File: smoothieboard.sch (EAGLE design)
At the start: 235 parts, among them IC1 LPC1769, IC10 LM1117-3.3V, IC11 78L12F, IC2 A4982, IC3 A4982, IC4 MCP44X1, IC5 A4982, IC6 A4982, J10 POWER_JACKSMD, Q1 BSL207SP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

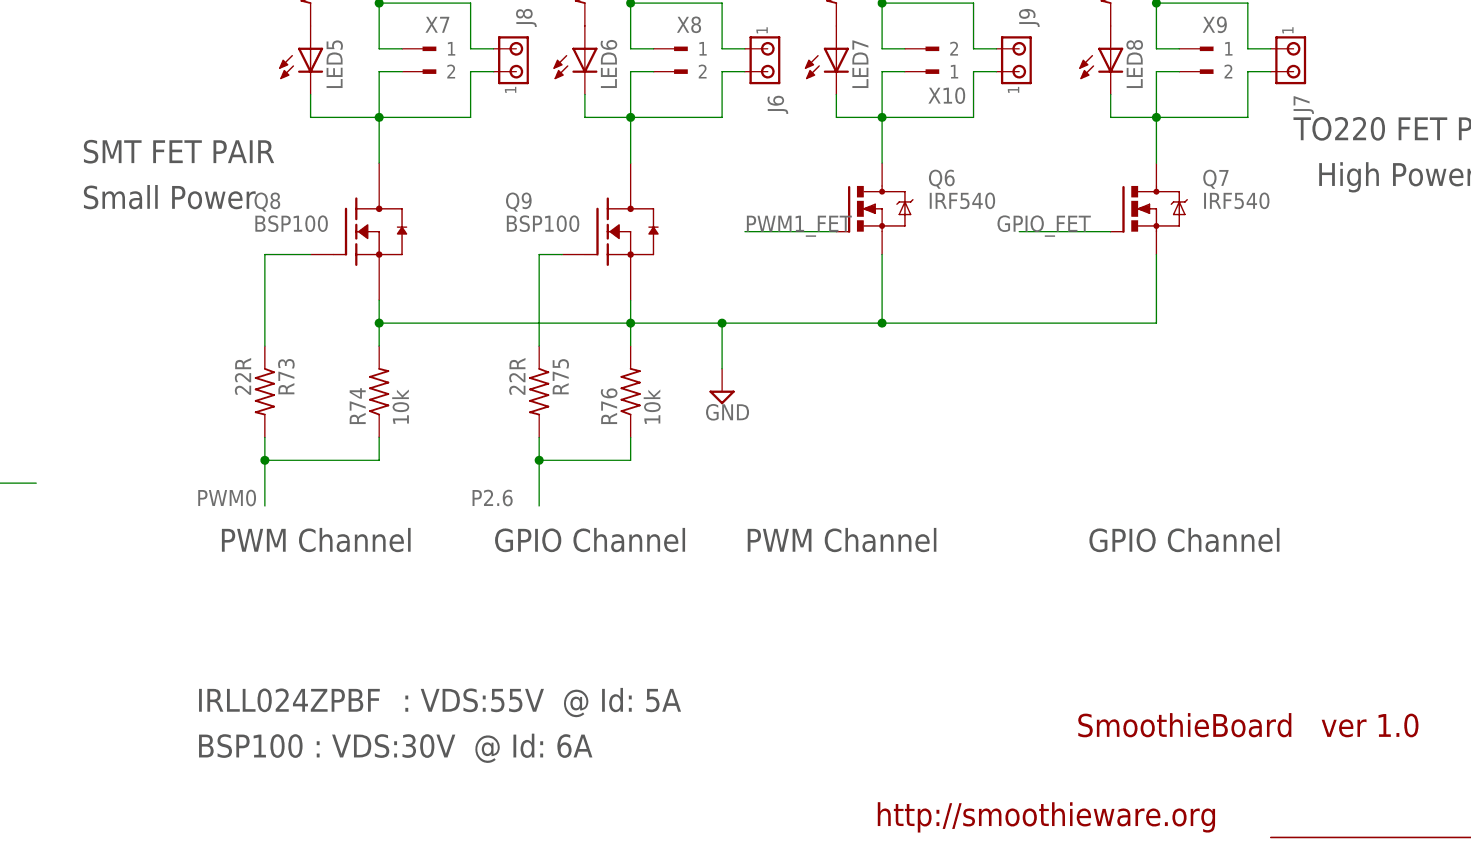
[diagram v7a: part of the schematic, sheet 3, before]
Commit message: Fixed MOSFET labels on schematic to match BOM
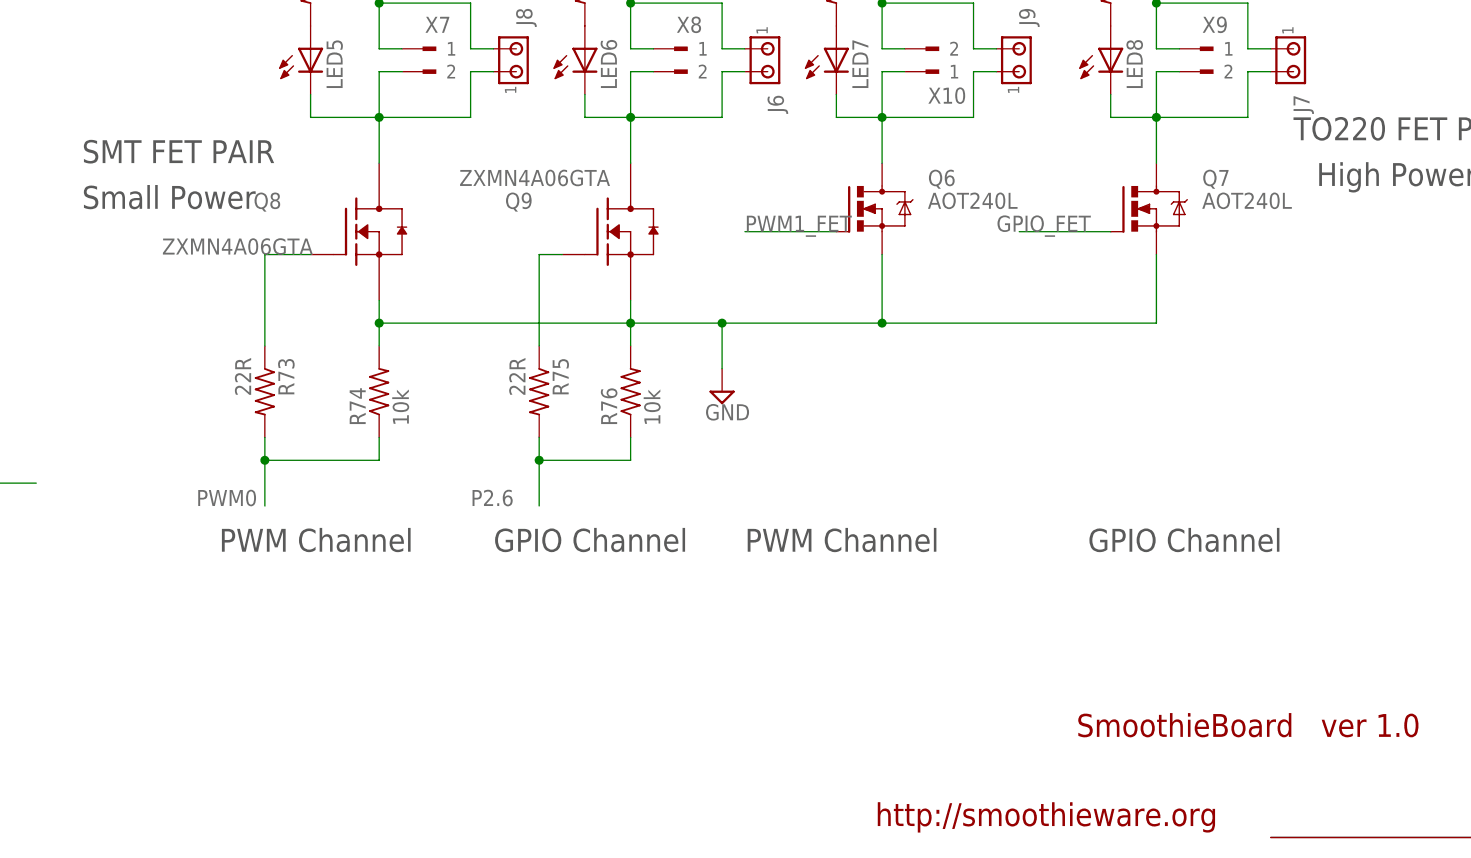
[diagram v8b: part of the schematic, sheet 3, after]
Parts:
- Q6, Q7: value IRF540 -> AOT240L
- Q8, Q9: value BSP100 -> ZXMN4A06GTA
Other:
- note removed: ": VDS:55V @ Id: 5A"
- note removed: "BSP100 : VDS:30V @ Id: 6A"
- note removed: "IRLL024ZPBF"
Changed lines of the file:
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@@
 <part name="LED9" library="led" deviceset="LED" device="CHIP-LED0805"/>
 <part name="R77" library="resistor" deviceset="R-US_" device="R0603" value="1k"/>
-<part name="Q6" library="transistor-power" deviceset="IRF540" device=""/>
-<part name="Q7" library="transistor-power" deviceset="IRF540" device=""/>
+<part name="Q6" library="transistor-power" deviceset="IRF540" device="" value="AOT240L"/>
+<part name="Q7" library="transistor-power" deviceset="IRF540" device="" value="AOT240L"/>
 <part name="SUPPLY18" library="supply2" deviceset="GND" device=""/>
 <part name="R73" library="resistor" deviceset="R-US_" device="R0603" value="22R"/>
@@
 <part name="R78" library="resistor" deviceset="R-US_" device="R0603" value="2.2K"/>
 <part name="LED10" library="led" deviceset="LED" device="CHIP-LED0805"/>
-<part name="Q8" library="ipc-7351-transistor" deviceset="MOSFET-NCH_" device="SOT-223" value="BSP100"/>
-<part name="Q9" library="ipc-7351-transistor" deviceset="MOSFET-NCH_" device="SOT-223" value="BSP100"/>
+<part name="Q8" library="ipc-7351-transistor" deviceset="MOSFET-NCH_" device="SOT-223" value="ZXMN4A06GTA"/>
+<part name="Q9" library="ipc-7351-transistor" deviceset="MOSFET-NCH_" device="SOT-223" value="ZXMN4A06GTA"/>
 <part name="R74" library="resistor" deviceset="R-US_" device="R0603" value="10k"/>
 <part name="R76" library="resistor" deviceset="R-US_" device="R0603" value="10k"/>
@@
 <text x="322.58" y="35.56" size="2.54" layer="97">GPIO Channel</text>
 <text x="284.48" y="35.56" size="2.54" layer="97">PWM Channel</text>
-<text x="223.52" y="17.78" size="2.54" layer="97">IRLL024ZPBF </text>
-<text x="246.38" y="17.78" size="2.54" layer="97">: VDS:55V  @ Id: 5A</text>
-<text x="223.52" y="12.7" size="2.54" layer="97">BSP100 : VDS:30V  @ Id: 6A</text>
 <text x="321.31" y="14.986" size="2.54" layer="94">SmoothieBoard   ver 1.0</text>
 <text x="298.958" y="5.08" size="2.54" layer="94">http://smoothieware.org</text>
@@
 <instance part="R78" gate="G$1" x="187.96" y="35.56" rot="R90"/>
 <instance part="LED10" gate="G$1" x="187.96" y="25.4"/>
-<instance part="Q8" gate="G$1" x="238.76" y="71.12"/>
-<instance part="Q9" gate="G$1" x="266.7" y="71.12"/>
+<instance part="Q8" gate="G$1" x="238.76" y="71.12" smashed="yes">
+<attribute name="VALUE" x="219.71" y="68.58" size="1.778" layer="96"/>
+<attribute name="NAME" x="229.87" y="73.66" size="1.778" layer="95"/>
+</instance>
+<instance part="Q9" gate="G$1" x="266.7" y="71.12" smashed="yes">
+<attribute name="VALUE" x="252.73" y="76.2" size="1.778" layer="96"/>
+<attribute name="NAME" x="257.81" y="73.66" size="1.778" layer="95"/>
+</instance>
 <instance part="R74" gate="G$1" x="243.84" y="53.34" rot="R90"/>
 <instance part="R76" gate="G$1" x="271.78" y="53.34" rot="R90"/>
